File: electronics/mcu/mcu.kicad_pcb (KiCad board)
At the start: 2 copper layers, 11 parts, among them IC1 ATTINY2313-S, P1 3.3v, P2 CONTROL, P3 SPI, P4 EXTRA, X1 8MHz

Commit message: finish the pcb
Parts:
- added Hole: VAL**, Pin_Headers:Pin_Header_Straight_1x01, F.Cu at (106.2, 120.9)
- added Hole: VAL**, Pin_Headers:Pin_Header_Straight_1x01, F.Cu at (106.2, 150.4)
- added Hole: VAL**, Pin_Headers:Pin_Header_Straight_1x01, F.Cu at (139.2, 150.4)
- added Hole: VAL**, Pin_Headers:Pin_Header_Straight_1x01, F.Cu at (139.2, 120.9)
- P4: footprint Pin_Headers:Pin_Header_Straight_2x07 -> Pin_Headers:Pin_Header_Straight_2x06
- X1: footprint QMONTRE_P:QMONTRE_P -> HC-49V_S:HC-49V_S
- moved C2 56.2 mm to (112.8, 143.8), turned to 270 degrees
- moved P1 49.5 mm to (106.7, 140.0), turned to 90 degrees
- moved P3 48.9 mm to (110.2, 133.6), turned to 270 degrees
- moved R1 48.0 mm to (113.8, 133.6), turned to 90 degrees
- moved C3 46.1 mm to (132.1, 138.4), turned to 270 degrees
- moved C1 41.6 mm to (119.9, 144.3), turned to 270 degrees
- moved C4 29.2 mm to (132.1, 128.3), turned to 90 degrees
- moved P2 28.1 mm to (129.5, 146.8)
- moved P4 20.6 mm to (121.9, 122.4)
- moved X1 13.5 mm to (137.2, 133.3), turned to 90 degrees
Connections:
- IC1 pad 11: Net-(IC1-Pad11) -> (no net)
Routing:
- net GND: track 0.00 -> 44.8 mm
- net Net-(C1-Pad1): track 0.00 -> 22.5 mm
- net Net-(C3-Pad1): track 0.00 -> 21.0 mm
- net Net-(C4-Pad1): track 0.00 -> 17.2 mm
- net Net-(IC1-Pad17): track 0.00 -> 15.9 mm
- net Net-(IC1-Pad18): track 0.00 -> 12.5 mm
- net Net-(IC1-Pad12): track 0.00 -> 11.3 mm
- net Net-(IC1-Pad13): track 0.00 -> 10.7 mm
- net Net-(IC1-Pad14): track 0.00 -> 10.2 mm
- net Net-(IC1-Pad15): track 0.00 -> 9.69 mm
- net Net-(IC1-Pad19): track 0.00 -> 9.46 mm
- net Net-(IC1-Pad16): track 0.00 -> 9.16 mm
- net Net-(IC1-Pad1): track 0.00 -> 6.60 mm
- net Net-(IC1-Pad2): track 0.00 -> 6.47 mm
- net Net-(IC1-Pad6): track 0.00 -> 6.47 mm
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- added copper zone on B.Cu, net GND
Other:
- net class Default: trace_width 0.25 -> 0.6; via_dia 0.6 -> 2.2; via_drill 0.4 -> 0.8

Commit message: finish the PCB
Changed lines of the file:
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@@
     (links 42)
     (no_connects 1)
-    (area 0 0 0 0)
+    (area 101.182333 118.271999 142.3892 152.908001)
     (thickness 1.6)
     (drawings 0)
@@
   )
   (setup
-    (last_trace_width 0.6)
+    (last_trace_width 0.8)
     (user_trace_width 0.8)
     (user_trace_width 1)
@@
     (mod_text_size 1 1)
     (mod_text_width 0.15)
-    (pad_size 3 3)
-    (pad_drill 2.5)
+    (pad_size 0.8 1.8)
+    (pad_drill 0)
     (pad_to_mask_clearance 0.2)
     (aux_axis_origin 0 0)
     (visible_elements FFFFFF7F)
     (pcbplotparams
-      (layerselection 0x00030_80000001)
+      (layerselection 0x00000_80000000)
       (usegerberextensions false)
       (excludeedgelayer true)
@@
       (padsonsilk false)
       (subtractmaskfromsilk false)
-      (outputformat 1)
+      (outputformat 5)
       (mirror false)
       (drillshape 1)
@@
     (fp_line (start -5.08 0.635) (end -5.08 -0.635) (layer B.SilkS) (width 0.15))
     (fp_line (start -5.08 -0.635) (end -6.35 -0.635) (layer B.SilkS) (width 0.15))
-    (pad 11 smd rect (at 5.715 4.826) (size 0.6 1.8) (layers B.Cu B.Paste B.Mask))
-    (pad 12 smd rect (at 4.445 4.826) (size 0.6 1.8) (layers B.Cu B.Paste B.Mask)
+    (pad 11 smd rect (at 5.715 4.826) (size 0.8 1.8) (layers B.Cu B.Paste B.Mask))
+    (pad 12 smd rect (at 4.445 4.826) (size 0.8 1.8) (layers B.Cu B.Paste B.Mask)
       (net 5 "Net-(IC1-Pad12)"))
-    (pad 13 smd rect (at 3.175 4.826) (size 0.6 1.8) (layers B.Cu B.Paste B.Mask)
+    (pad 13 smd rect (at 3.175 4.826) (size 0.8 1.8) (layers B.Cu B.Paste B.Mask)
       (net 6 "Net-(IC1-Pad13)"))
-    (pad 14 smd rect (at 1.905 4.826) (size 0.6 1.8) (layers B.Cu B.Paste B.Mask)
+    (pad 14 smd rect (at 1.905 4.826) (size 0.8 1.8) (layers B.Cu B.Paste B.Mask)
       (net 7 "Net-(IC1-Pad14)"))
-    (pad 15 smd rect (at 0.635 4.826) (size 0.6 1.8) (layers B.Cu B.Paste B.Mask)
+    (pad 15 smd rect (at 0.635 4.826) (size 0.8 1.8) (layers B.Cu B.Paste B.Mask)
       (net 8 "Net-(IC1-Pad15)"))
-    (pad 16 smd rect (at -0.635 4.826) (size 0.6 1.8) (layers B.Cu B.Paste B.Mask)
+    (pad 16 smd rect (at -0.635 4.826) (size 0.8 1.8) (layers B.Cu B.Paste B.Mask)
       (net 9 "Net-(IC1-Pad16)"))
-    (pad 17 smd rect (at -1.905 4.826) (size 0.6 1.8) (layers B.Cu B.Paste B.Mask)
+    (pad 17 smd rect (at -1.905 4.826) (size 0.8 1.8) (layers B.Cu B.Paste B.Mask)
       (net 10 "Net-(IC1-Pad17)"))
-    (pad 18 smd rect (at -3.175 4.826) (size 0.6 1.8) (layers B.Cu B.Paste B.Mask)
+    (pad 18 smd rect (at -3.175 4.826) (size 0.8 1.8) (layers B.Cu B.Paste B.Mask)
       (net 11 "Net-(IC1-Pad18)"))
-    (pad 19 smd rect (at -4.445 4.826) (size 0.6 1.8) (layers B.Cu B.Paste B.Mask)
+    (pad 19 smd rect (at -4.445 4.826) (size 0.8 1.8) (layers B.Cu B.Paste B.Mask)
       (net 12 "Net-(IC1-Pad19)"))
-    (pad 20 smd rect (at -5.715 4.826) (size 0.6 1.8) (layers B.Cu B.Paste B.Mask)
+    (pad 20 smd rect (at -5.715 4.826) (size 0.8 1.8) (layers B.Cu B.Paste B.Mask)
       (net 1 "Net-(C1-Pad1)"))
-    (pad 1 smd rect (at -5.715 -4.826) (size 0.6 1.8) (layers B.Cu B.Paste B.Mask)
+    (pad 1 smd rect (at -5.715 -4.826) (size 0.8 1.8) (layers B.Cu B.Paste B.Mask)
       (net 13 "Net-(IC1-Pad1)"))
-    (pad 2 smd rect (at -4.445 -4.826) (size 0.6 1.8) (layers B.Cu B.Paste B.Mask)
+    (pad 2 smd rect (at -4.445 -4.826) (size 0.8 1.8) (layers B.Cu B.Paste B.Mask)
       (net 14 "Net-(IC1-Pad2)"))
-    (pad 3 smd rect (at -3.175 -4.826) (size 0.6 1.8) (layers B.Cu B.Paste B.Mask)
+    (pad 3 smd rect (at -3.175 -4.826) (size 0.8 1.8) (layers B.Cu B.Paste B.Mask)
       (net 15 "Net-(IC1-Pad3)"))
-    (pad 4 smd rect (at -1.905 -4.826) (size 0.6 1.8) (layers B.Cu B.Paste B.Mask)
+    (pad 4 smd rect (at -1.905 -4.826) (size 0.8 1.8) (layers B.Cu B.Paste B.Mask)
       (net 3 "Net-(C3-Pad1)"))
-    (pad 5 smd rect (at -0.635 -4.826) (size 0.6 1.8) (layers B.Cu B.Paste B.Mask)
+    (pad 5 smd rect (at -0.635 -4.826) (size 0.8 1.8) (layers B.Cu B.Paste B.Mask)
       (net 4 "Net-(C4-Pad1)"))
-    (pad 6 smd rect (at 0.635 -4.826) (size 0.6 1.8) (layers B.Cu B.Paste B.Mask)
+    (pad 6 smd rect (at 0.635 -4.826) (size 0.8 1.8) (layers B.Cu B.Paste B.Mask)
       (net 16 "Net-(IC1-Pad6)"))
-    (pad 7 smd rect (at 1.905 -4.826) (size 0.6 1.8) (layers B.Cu B.Paste B.Mask)
+    (pad 7 smd rect (at 1.905 -4.826) (size 0.8 1.8) (layers B.Cu B.Paste B.Mask)
       (net 17 "Net-(IC1-Pad7)"))
-    (pad 8 smd rect (at 3.175 -4.826) (size 0.6 1.8) (layers B.Cu B.Paste B.Mask)
+    (pad 8 smd rect (at 3.175 -4.826) (size 0.8 1.8) (layers B.Cu B.Paste B.Mask)
       (net 18 "Net-(IC1-Pad8)"))
-    (pad 9 smd rect (at 4.445 -4.826) (size 0.6 1.8) (layers B.Cu B.Paste B.Mask)
+    (pad 9 smd rect (at 4.445 -4.826) (size 0.8 1.8) (layers B.Cu B.Paste B.Mask)
       (net 19 "Net-(IC1-Pad9)"))
-    (pad 10 smd rect (at 5.715 -4.826) (size 0.6 1.8) (layers B.Cu B.Paste B.Mask)
+    (pad 10 smd rect (at 5.715 -4.826) (size 0.8 1.8) (layers B.Cu B.Paste B.Mask)
       (net 2 GND))
     (model SMD_Packages/SO-20-L.wrl
@@
     )
   )
-  (segment (start 116.84 138.176) (end 114.3 138.176) (width 0.6) (layer B.Cu) (net 1))
+  (segment (start 116.84 138.176) (end 114.3 138.176) (width 0.8) (layer B.Cu) (net 1))
   (segment (start 114.3 138.176) (end 113.792 138.684) (width 0.6) (layer B.Cu) (net 1))
   (segment (start 119.888 141.732) (end 113.792 141.732) (width 0.8) (layer B.Cu) (net 1))
@@
   (segment (start 113.792 141.732) (end 113.792 142.748) (width 0.8) (layer B.Cu) (net 1))
   (segment (start 113.792 142.748) (end 112.776 143.764) (width 0.8) (layer B.Cu) (net 1))
-  (segment (start 128.27 128.524) (end 131.064 128.524) (width 0.6) (layer B.Cu) (net 2))
+  (segment (start 128.27 128.524) (end 131.064 128.524) (width 0.8) (layer B.Cu) (net 2))
   (segment (start 128.27 121.158) (end 131.318 121.158) (width 0.8) (layer B.Cu) (net 2))
   (segment (start 131.318 121.158) (end 131.572 120.904) (width 0.8) (layer B.Cu) (net 2))

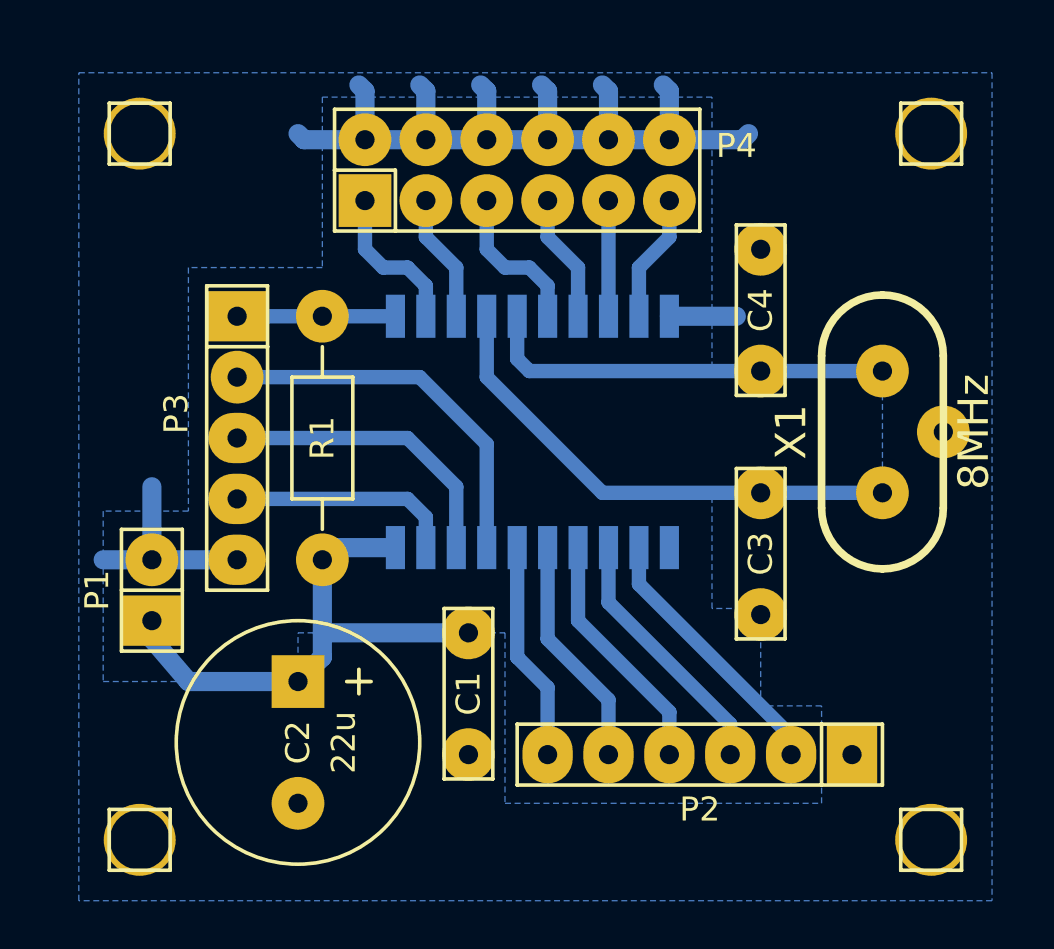
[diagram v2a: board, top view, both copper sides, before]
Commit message: join uart and spi on the mcu pcb
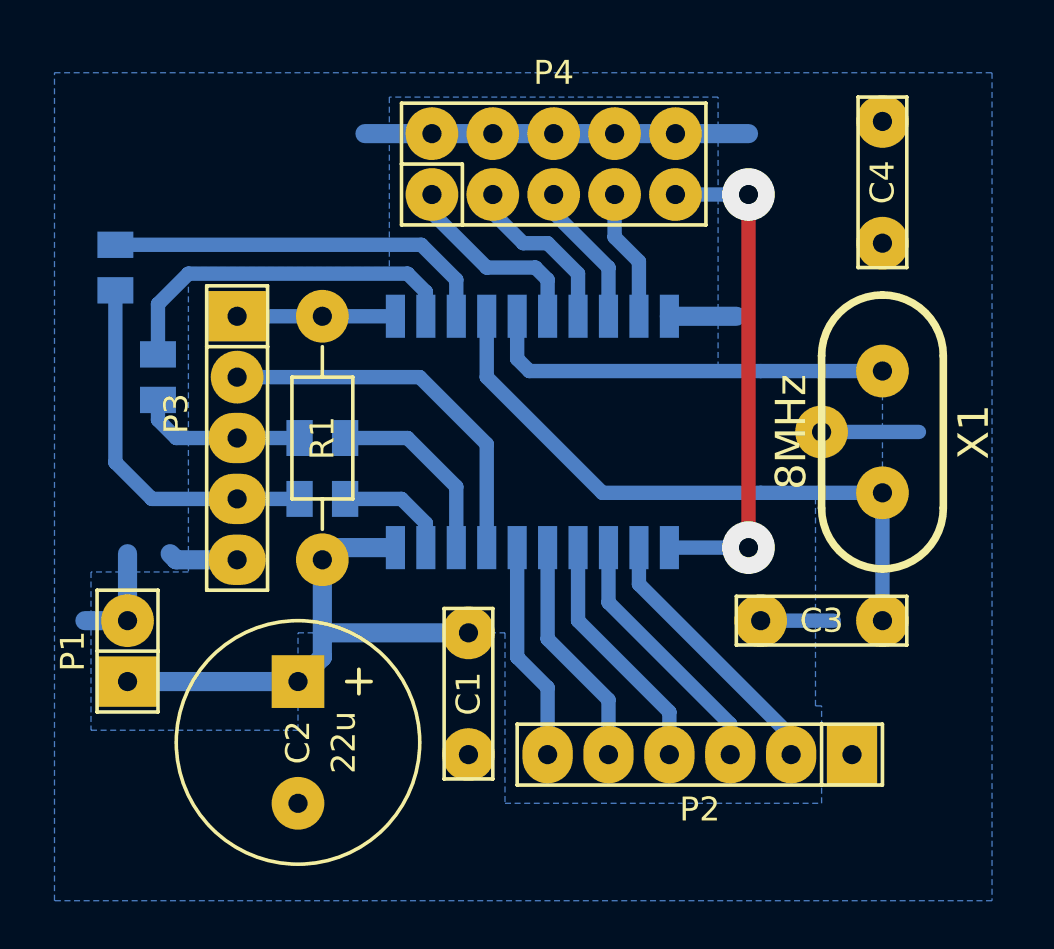
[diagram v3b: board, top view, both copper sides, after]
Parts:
- removed Hole (x4): VAL**, Pin_Headers:Pin_Header_Straight_1x01
- added R2: 100, Resistors_SMD:R_0805, B.Cu at (113.8, 133.6)
- added R3: 100, Resistors_SMD:R_0805, B.Cu at (113.8, 136.1)
- added R4: 100, Resistors_SMD:R_0805, B.Cu at (106.9, 131.1)
- added R5: 100, Resistors_SMD:R_0805, B.Cu at (105.2, 126.5)
- P3: value SPI -> PI
- P4: footprint Pin_Headers:Pin_Header_Straight_2x06 -> Pin_Headers:Pin_Header_Straight_2x05
- moved C4 7.37 mm to (137.2, 122.9)
- moved C3 3.78 mm to (134.6, 141.2), turned to 180 degrees
- moved P1 2.74 mm to (105.7, 142.5)
- moved P4 1.55 mm to (123.4, 122.2)
- turned X1 to 270 degrees
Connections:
- IC1 pad 11: (no net) -> Net-(IC1-Pad11)
- P3 pad 3: Net-(IC1-Pad18) -> Net-(P3-Pad3)
- P3 pad 4: Net-(IC1-Pad19) -> Net-(P3-Pad4)
- P4 pad 1: Net-(IC1-Pad2) -> Net-(IC1-Pad6)
- P4 pad 3: Net-(IC1-Pad3) -> Net-(IC1-Pad7)
- P4 pad 5: Net-(IC1-Pad6) -> Net-(IC1-Pad8)
- P4 pad 7: Net-(IC1-Pad7) -> Net-(IC1-Pad9)
- P4 pad 9: Net-(IC1-Pad8) -> Net-(IC1-Pad11)
- X1 pad 1: Net-(C3-Pad1) -> Net-(C4-Pad1)
- X1 pad 2: Net-(C4-Pad1) -> Net-(C3-Pad1)
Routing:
- net Net-(IC1-Pad11): track 0.00 -> 21.1 mm, vias 0 -> 2
- net Net-(P3-Pad4): track 0.00 -> 15.5 mm
- net GND: track 44.8 -> 33.4 mm
- net Net-(IC1-Pad3): track 5.35 -> 16.4 mm
- net Net-(IC1-Pad2): track 6.47 -> 15.1 mm
- net Net-(P3-Pad3): track 0.00 -> 7.05 mm
- net Net-(C3-Pad1): track 21.0 -> 26.4 mm
- net Net-(IC1-Pad19): track 9.46 -> 4.80 mm
- net Net-(IC1-Pad18): track 12.5 -> 8.02 mm
- net Net-(IC1-Pad6): track 6.47 -> 8.27 mm
- net Net-(IC1-Pad7): track 5.35 -> 7.15 mm
- net Net-(IC1-Pad8): track 4.83 -> 6.03 mm
- net Net-(C1-Pad1): track 22.5 -> 22.0 mm
